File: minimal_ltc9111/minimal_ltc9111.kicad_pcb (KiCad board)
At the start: 4 copper layers, 22.9 x 41.9 mm, 24 parts, among them Q1 100 V, Q2 100 V, Q3 100 V, Q4 100.0 V, U1 LTC9111RDE-PBF

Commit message: Backup
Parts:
- added J1: FW-02-03-G-D-085-155, connector_footprints:FW-02-03-G-D-085-155, F.Cu at (153.9, 80.5)
- added J2: FW-02-03-G-D-085-155, connector_footprints:FW-02-03-G-D-085-155, F.Cu at (153.9, 133.8)
- added MB1: mouse-bite-midle-50mil-200mil, mouse_bite_footprints:mouse-bite-midle-50mil-200mil, F.Cu at (153.9, 83.0)
- added MB2: mouse-bite-midle-50mil-200mil, mouse_bite_footprints:mouse-bite-midle-50mil-200mil, F.Cu at (153.9, 131.3)
- added TP1: TestPoint, test_point_footprints:TestPoint_THTPad_Castelated, F.Cu at (153.3, 83.7)
- added TP2: TestPoint, test_point_footprints:TestPoint_THTPad_Castelated, F.Cu at (154.6, 83.7)
- added TP3: TestPoint, test_point_footprints:TestPoint_THTPad_Castelated, F.Cu at (154.6, 130.7)
- added TP4: TestPoint, test_point_footprints:TestPoint_THTPad_Castelated, F.Cu at (153.3, 130.7)
- moved C8 1.02 mm to (161.0, 115.0)
- moved C6 1.02 mm to (157.6, 115.0)
- moved R5 0.51 mm to (155.9, 103.7)
- moved C7 0.51 mm to (160.0, 103.7)
- moved D1 0.39 mm to (150.5, 102.7)
- moved C4 0.39 mm to (155.7, 101.8)
- moved R1 0.31 mm to (147.2, 106.2)
- moved R2 0.31 mm to (149.5, 106.2)
- moved R3 0.25 mm to (153.9, 118.0)
- moved C1 0.25 mm to (150.0, 122.3)
- moved C5 0.25 mm to (157.8, 122.3)
- moved D2 0.25 mm to (151.4, 99.7)
- moved D3 0.25 mm to (156.4, 99.7)
- moved Q2 0.25 mm to (147.8, 109.4)
- moved Q3 0.25 mm to (150.1, 109.4)
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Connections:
- L1 pad 2: unconnected-(L1-Pad2) -> /POWER_IN_N
- L1 pad 3: unconnected-(L1-Pad3) -> /POWER_IN_P
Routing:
- net GND: track 0.76 -> 3.56 mm, vias 11 -> 43
- net /POWER_IN_P: vias 0 -> 5
- net /POWER_IN_N: vias 0 -> 5
- net /OUT: vias 0 -> 8
- net /BULK_OUT: vias 0 -> 3
- added copper zone on In1.Cu, net /BULK_OUT
- added copper zone on B.Cu, net /IN
- added copper zone on In1.Cu, net /IN
- added copper zone on In1.Cu, net /OUT
- added copper zone on F.Cu, net /POWER_IN_N
- added copper zone on In1.Cu, net /POWER_IN_N
- added copper zone on F.Cu, net /POWER_IN_P
- added copper zone on In1.Cu, net /POWER_IN_P
- added copper zone on B.Cu, net /POWER_N
- added copper zone on B.Cu, net /POWER_P
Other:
- board size 22.9 x 41.9 mm -> 22.9 x 59.7 mm

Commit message: Backup
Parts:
- moved C8 3.74 mm to (157.3, 115.0), turned to 90 degrees
- moved C9 3.49 mm to (160.9, 107.6), turned to 90 degrees
- moved C6 3.16 mm to (160.8, 115.0), turned to 90 degrees
- moved C1 1.27 mm to (150.0, 123.6)
- moved C5 1.27 mm to (157.8, 123.6)
- moved R3 1.27 mm to (153.9, 119.2)
- moved Q1 1.02 mm to (148.9, 114.1)
- moved C3 0.13 mm to (154.2, 112.4)
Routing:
- net GND: track 3.56 -> 5.33 mm, vias 43 -> 41
- net /LGATE2: track 3.86 -> 3.00 mm
- net /BULK_OUT: vias 3 -> 15
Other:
- board size 22.9 x 59.7 mm -> 19.1 x 59.7 mm

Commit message: Backup
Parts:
- moved J2 38.1 mm to (128.9, 105.2), turned to 180 degrees
- moved J1 37.6 mm to (182.2, 105.2), turned to 0 degrees
- moved MB2 34.5 mm to (131.5, 105.2), turned to 90 degrees
- moved MB1 34.0 mm to (179.7, 105.2), turned to -90 degrees
- moved TP4 33.7 mm to (132.1, 104.5), turned to 0 degrees
- moved TP3 33.5 mm to (132.1, 105.8), turned to 0 degrees
- moved TP1 33.2 mm to (179.1, 104.5), turned to 180 degrees
- moved TP2 33.0 mm to (179.1, 105.8), turned to 180 degrees
- moved C1 24.8 mm to (139.2, 101.3), turned to 180 degrees
- moved C5 23.7 mm to (139.2, 109.1), turned to 180 degrees
- moved L1 22.1 mm to (171.3, 105.2), turned to 90 degrees
- moved R3 17.5 mm to (143.5, 105.2), turned to 180 degrees
- moved C2 14.1 mm to (165.1, 103.4), turned to 90 degrees
- moved Q1 14.0 mm to (148.7, 100.1), turned to 90 degrees
- moved C6 13.4 mm to (147.7, 112.0), turned to 0 degrees
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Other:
- board size 19.1 x 59.7 mm -> 59.7 x 19 mm

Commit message: Backup
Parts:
- C6, C8: footprint capacitor_footprints:C_1210_3225Metric -> capacitor_footprints:C_1210_200_3225Metric
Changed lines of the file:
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@@
 		)
 	)
-	(footprint "capacitor_footprints:C_1210_3225Metric"
+	(footprint "capacitor_footprints:C_1210_200_3225Metric"
 		(layer "F.Cu")
 		(at 147.735077 108.533755)
 		(property "Reference" "C8"
-			(at -2.1572 -0.608838 0)
+			(at -2.294677 -0.609155 0)
 			(unlocked yes)
 			(layer "F.SilkS")
@@
 			)
 		)
-		(property "Footprint" "capacitor_footprints:C_1210_3225Metric"
+		(property "Footprint" "capacitor_footprints:C_1210_200_3225Metric"
 			(at 0 0 0)
 			(layer "F.Fab")
@@
 			)
 		)
-		(property "Description" "CAP SMD 4.7 µF X7S 10% 1210 100V"
+		(property "Description" "CAP SMD 4.7 µF X7S 10% 1210_200 100V"
 			(at 0 0 0)
 			(layer "F.Fab")
@@
 			)
 		)
-		(property "Case Code - in" "1210"
+		(property "Case Code - in" "1210_200"
 			(at 0 0 0)
 			(unlocked yes)
@@
 		)
 		(property "Voltage Rating" "100V"
+			(at 0 0 0)
+			(unlocked yes)
+			(layer "F.Fab")
+			(hide yes)
+			(effects
+				(font
+					(size 1 1)
+					(thickness 0.15)
+				)
+			)
+		)
+		(property "3dviewer Link" "https://3dviewer.net/index.html#model=https://github.com/ionutms/KiCAD_Symbols_Generator/blob/main/3D_models/C_1210.step"
+			(at 0 0 0)
+			(unlocked yes)
+			(layer "F.Fab")
+			(hide yes)
+			(effects
+				(font
+					(size 1 1)
+					(thickness 0.15)
+				)
+			)
+		)
+		(property "Capacitor Type" "Ceramic"
 			(at 0 0 0)
 			(unlocked yes)
@@
 			(net 16 "/OUT")
 			(pintype "unspecified")
-			(teardrops
-				(best_length_ratio 0.5)
-				(max_length 1)
-				(best_width_ratio 1)
-				(max_width 2)
-				(curve_points 5)
-				(filter_ratio 0.9)
-				(enabled yes)
-				(allow_two_segments yes)
-				(prefer_zone_connections yes)
-			)
 		)
 		(pad "2" smd roundrect
@@
 			(net 3 "GND")
 			(pintype "unspecified")
-			(teardrops
-				(best_length_ratio 0.5)
-				(max_length 1)
-				(best_width_ratio 1)
-				(max_width 2)
-				(curve_points 5)
-				(filter_ratio 0.9)
-				(enabled yes)
-				(allow_two_segments yes)
-				(prefer_zone_connections yes)
-			)
-		)
-		(model "${KIPRJMOD}/KiCAD_Symbol_Generator/3D_models/C_1210.step"
+		)
+		(model "${KIPRJMOD}/KiCAD_Symbol_Generator/3D_models/C_1210_200.step"
 			(offset
 				(xyz 0 0 0)
@@
 		)
 	)
-	(footprint "capacitor_footprints:C_1210_3225Metric"
+	(footprint "capacitor_footprints:C_1210_200_3225Metric"
 		(layer "F.Cu")
 		(at 147.735077 111.986885)
 		(property "Reference" "C6"
-			(at -2.1572 -0.912368 0)
+			(at -2.243877 -0.912685 0)
 			(unlocked yes)
 			(layer "F.SilkS")
@@
 			)
 		)
-		(property "Footprint" "capacitor_footprints:C_1210_3225Metric"
+		(property "Footprint" "capacitor_footprints:C_1210_200_3225Metric"
 			(at 0 0 0)
 			(layer "F.Fab")
@@
 			)
 		)
-		(property "Description" "CAP SMD 4.7 µF X7S 10% 1210 100V"
+		(property "Description" "CAP SMD 4.7 µF X7S 10% 1210_200 100V"
 			(at 0 0 0)
 			(layer "F.Fab")
@@
 			)
 		)
-		(property "Case Code - in" "1210"
+		(property "Case Code - in" "1210_200"
 			(at 0 0 0)
 			(unlocked yes)
@@
 		)
 		(property "Voltage Rating" "100V"
+			(at 0 0 0)
+			(unlocked yes)
+			(layer "F.Fab")
+			(hide yes)
+			(effects
+				(font
+					(size 1 1)
+					(thickness 0.15)
+				)
+			)
+		)
+		(property "3dviewer Link" "https://3dviewer.net/index.html#model=https://github.com/ionutms/KiCAD_Symbols_Generator/blob/main/3D_models/C_1210.step"
+			(at 0 0 0)
+			(unlocked yes)
+			(layer "F.Fab")
+			(hide yes)
+			(effects
+				(font
+					(size 1 1)
+					(thickness 0.15)
+				)
+			)
+		)
+		(property "Capacitor Type" "Ceramic"
 			(at 0 0 0)
 			(unlocked yes)
@@
 			(net 16 "/OUT")
 			(pintype "unspecified")
-			(teardrops
-				(best_length_ratio 0.5)
-				(max_length 1)
-				(best_width_ratio 1)
-				(max_width 2)
-				(curve_points 5)
-				(filter_ratio 0.9)
-				(enabled yes)
-				(allow_two_segments yes)
-				(prefer_zone_connections yes)
-			)
 		)
 		(pad "2" smd roundrect
@@
 			(net 3 "GND")
 			(pintype "unspecified")
-			(teardrops
-				(best_length_ratio 0.5)
-				(max_length 1)
-				(best_width_ratio 1)
-				(max_width 2)
-				(curve_points 5)
-				(filter_ratio 0.9)
-				(enabled yes)
-				(allow_two_segments yes)
-				(prefer_zone_connections yes)
-			)
-		)
-		(model "${KIPRJMOD}/KiCAD_Symbol_Generator/3D_models/C_1210.step"
+		)
+		(model "${KIPRJMOD}/KiCAD_Symbol_Generator/3D_models/C_1210_200.step"
 			(offset
 				(xyz 0 0 0)

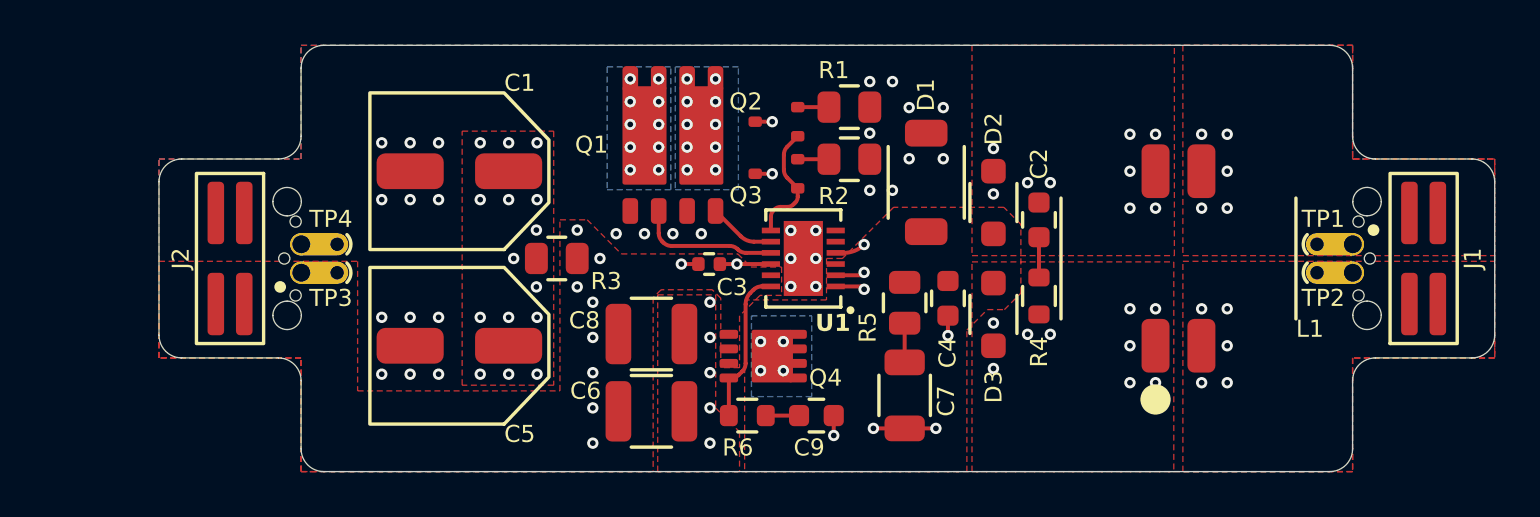
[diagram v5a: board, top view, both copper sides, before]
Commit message: Update subproject commit and fix component order in minimal_ltc9111.pdf
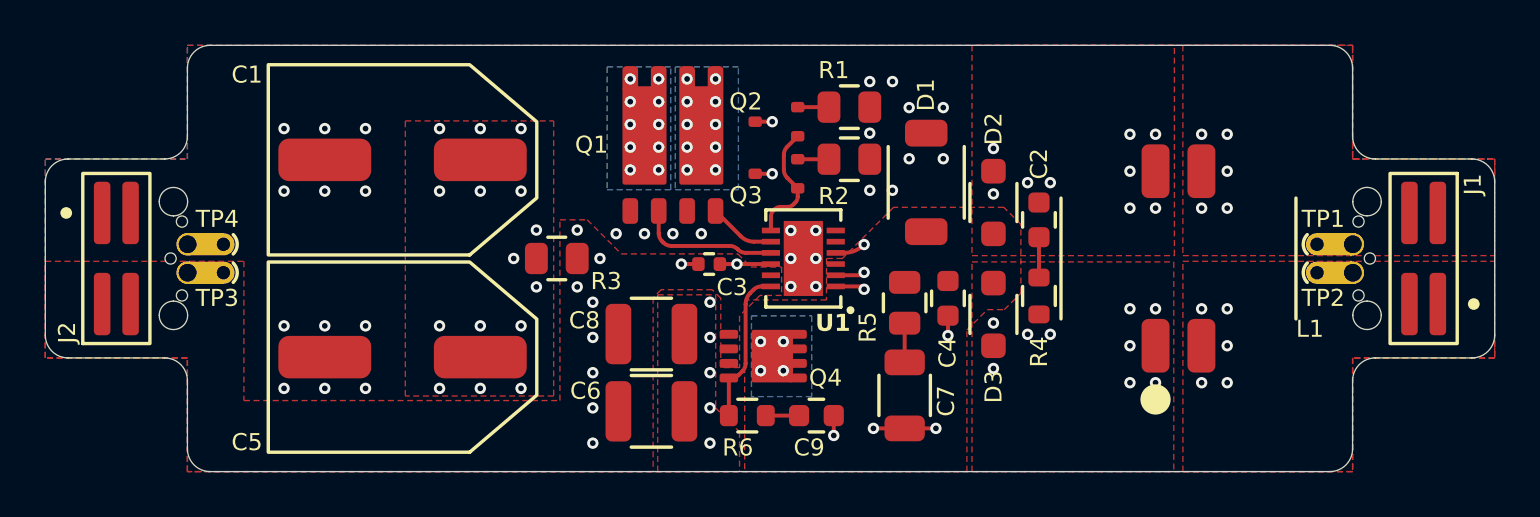
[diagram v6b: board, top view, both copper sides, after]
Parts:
- C1, C5: footprint capacitor_footprints:C_026x026x0236_6_6x6_6x6_0Metric -> capacitor_footprints:C_031x0468_8_0x11_9Metric
- moved J2 5.08 mm to (123.8, 105.2), turned to 0 degrees
- moved MB2 5.08 mm to (126.4, 105.2)
- moved TP3 5.08 mm to (127.0, 105.8)
- moved TP4 5.08 mm to (127.0, 104.5)
- moved C5 2.59 mm to (136.6, 109.6)
- moved C1 2.59 mm to (136.6, 100.7)
- turned J1 to 180 degrees
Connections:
- J1 pad 1: /POWER_IN_P -> /POWER_IN_N
- J1 pad 2: /POWER_IN_N -> /POWER_IN_P
- J1 pad 3: /POWER_IN_P -> /POWER_IN_N
- J1 pad 4: /POWER_IN_N -> /POWER_IN_P
- J2 pad 1: /OUT -> GND
- J2 pad 2: GND -> /OUT
- J2 pad 3: /OUT -> GND
- J2 pad 4: GND -> /OUT
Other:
- board size 59.7 x 19 mm -> 64.8 x 19 mm

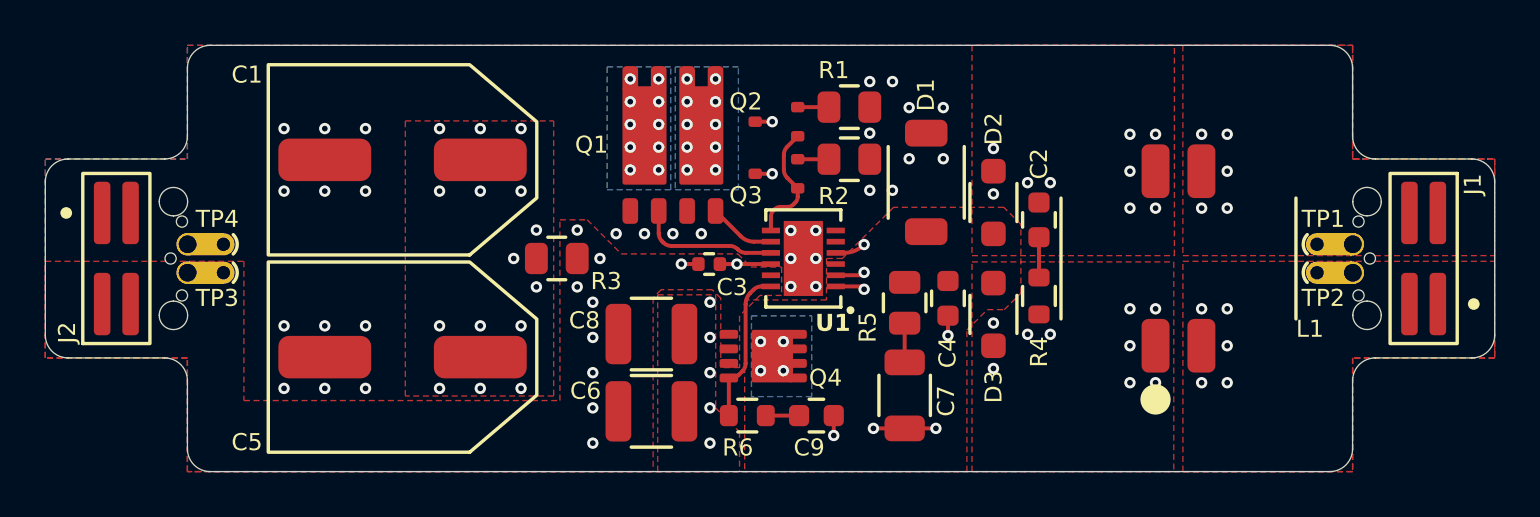
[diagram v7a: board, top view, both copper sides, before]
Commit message: Update subproject commit and enhance component blacklist in ibom.config.ini; add new libraries in fp-lib-table and sym-lib-table
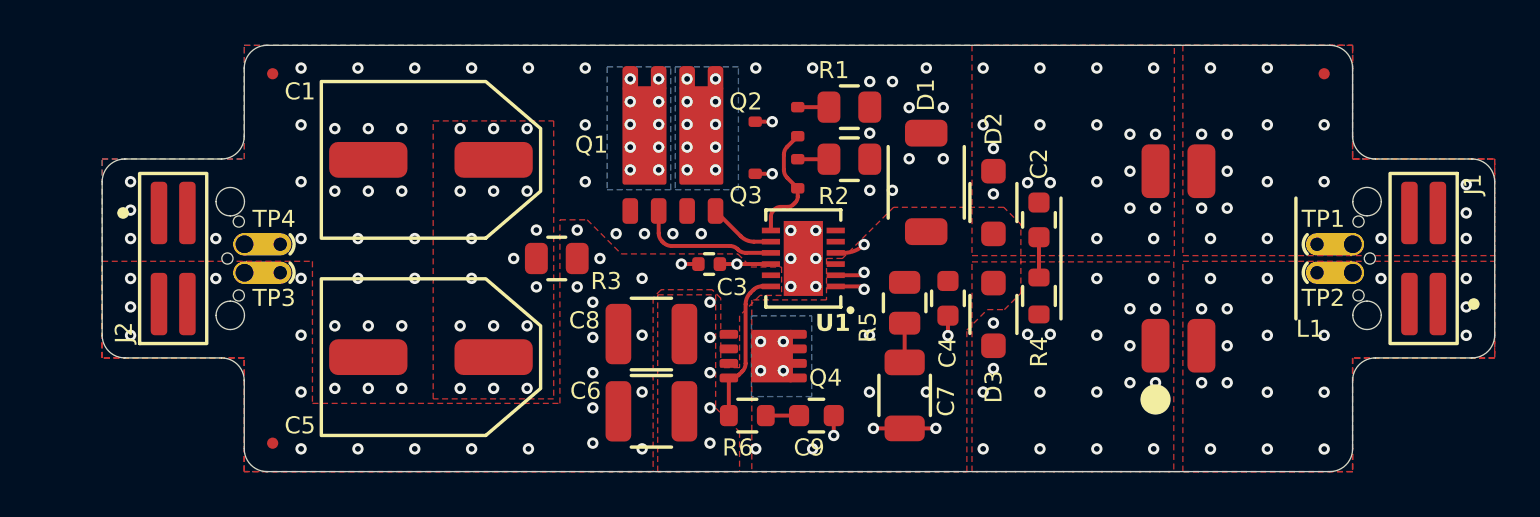
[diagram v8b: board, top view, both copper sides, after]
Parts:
- added FID1: Fiducial, no_components_footprints:Fiducial_0.5mm_Mask1mm, F.Cu at (130.8, 96.9)
- added FID2: Fiducial, no_components_footprints:Fiducial_0.5mm_Mask1mm, F.Cu at (130.8, 113.4)
- added FID3: Fiducial, no_components_footprints:Fiducial_0.5mm_Mask1mm, F.Cu at (177.8, 96.9)
- C1, C5: value 68 µF -> 22 µF; footprint capacitor_footprints:C_031x0468_8_0x11_9Metric -> capacitor_footprints:C_023x0248_5_9x6_3Metric
- moved J2 2.54 mm to (126.4, 105.2)
- moved MB2 2.54 mm to (128.9, 105.2)
- moved TP3 2.54 mm to (129.6, 105.8)
- moved TP4 2.54 mm to (129.6, 104.5)
- moved C1 1.27 mm to (137.9, 100.7)
- moved C5 1.27 mm to (137.9, 109.6)
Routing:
- net GND: vias 41 -> 68
- net /POWER_P: vias 21 -> 31
- net /POWER_N: vias 21 -> 31
- net /POWER_IN_P: vias 5 -> 17
- net /POWER_IN_N: vias 5 -> 18
- net /OUT: vias 8 -> 24
- net /BULK_OUT: vias 15 -> 17
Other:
- board size 64.8 x 19 mm -> 62.2 x 19 mm
